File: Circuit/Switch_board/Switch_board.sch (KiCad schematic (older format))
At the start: 10 parts

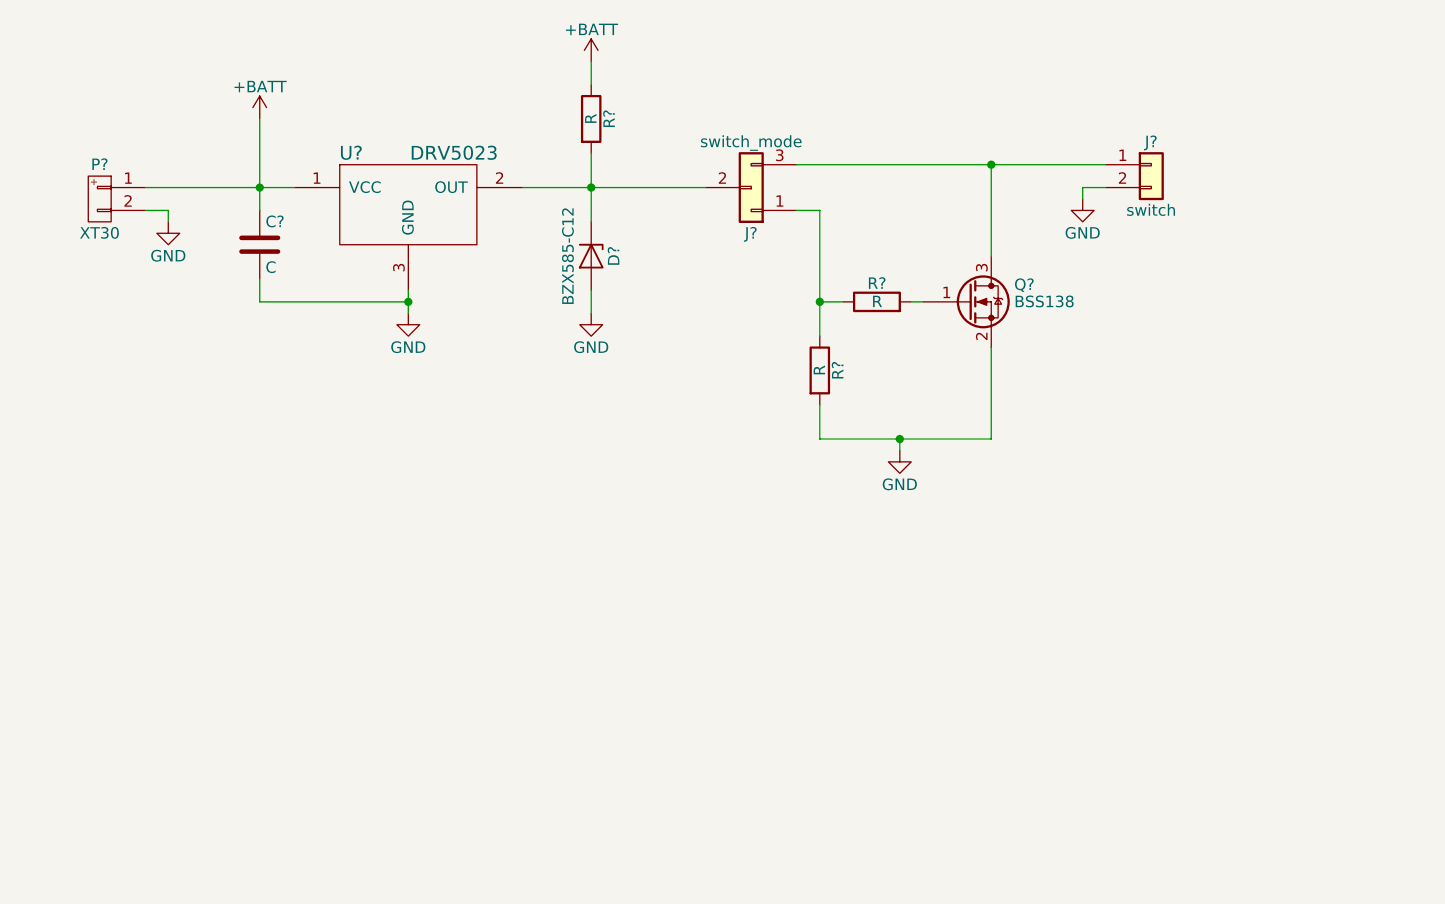
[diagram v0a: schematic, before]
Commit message: switch_board circuit could operate in any switch application without complex config
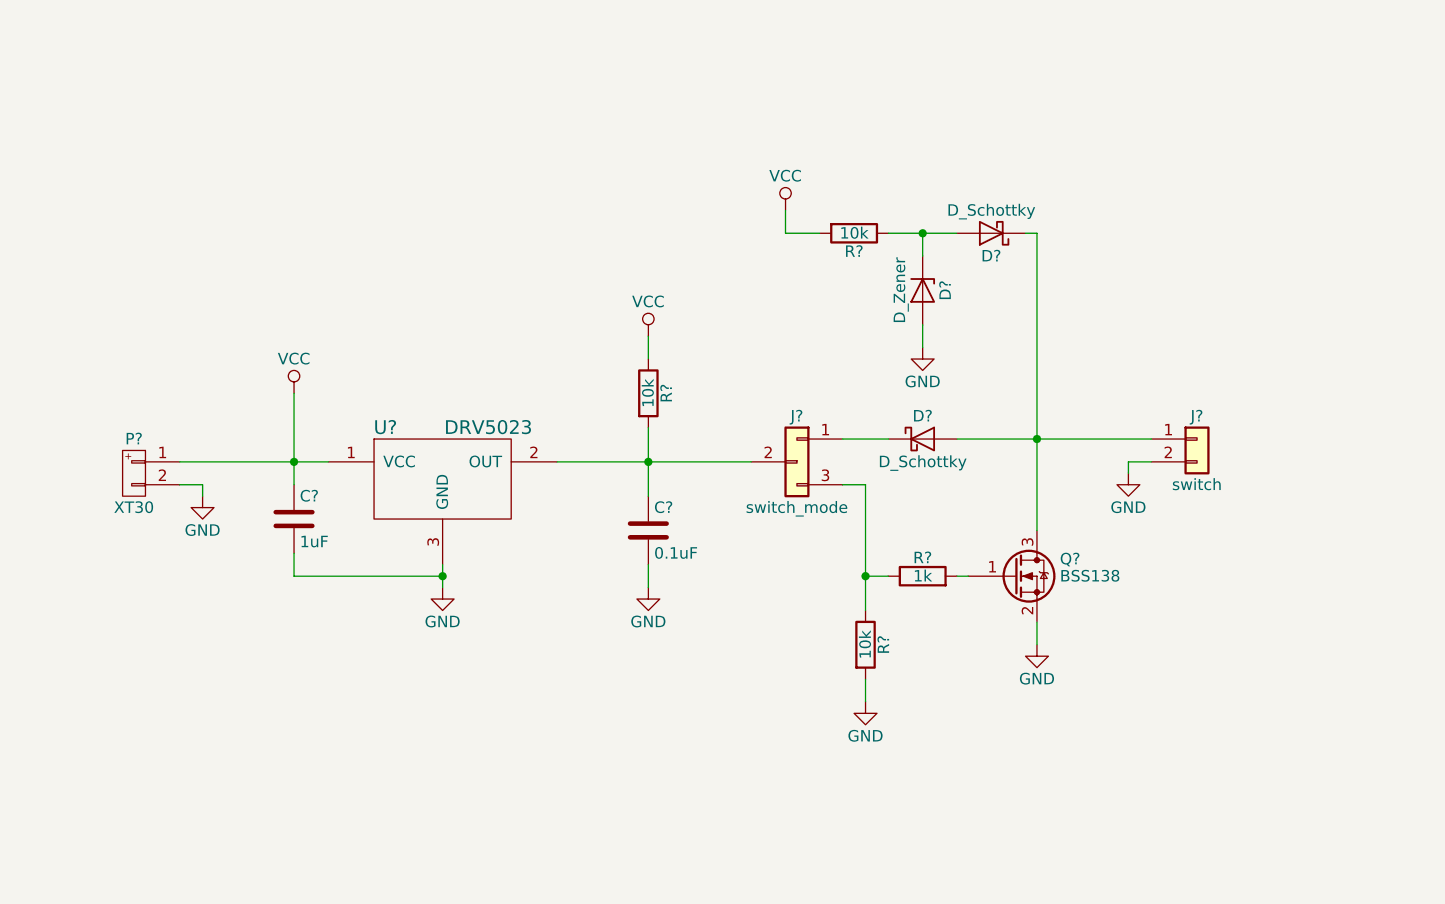
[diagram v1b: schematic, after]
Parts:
- removed D?: BZX585-C12, symbol D_Zener
- added C?: 0.1uF, symbol C
- added D?: D_Zener, symbol D_Zener
- added D? (x2): D_Schottky, symbol D_Schottky
- added R?: 10k, symbol R
- C?: value C -> 1uF
- R? (x2): value R -> 10k
- R?: value R -> 1k
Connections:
- net GND: now also C?.2, D?.2 (A)
- net at J?.2 (Pin_2), R?.2, U?.2 (OUT): now also C?.1
- net at R?.1, R?.1: now also J?.3 (Pin_3); no longer J?.1 (Pin_1)
- net at J?.1 (Pin_1), Q?.3 (D): now also D?.1 (K), D?.2 (A); no longer J?.3 (Pin_3)
- net +BATT renamed VCC
- net VCC: now also R?.2
- new net: D?.1 (K), J?.1 (Pin_1)
- new net: D?.1 (K), D?.2 (A), R?.1
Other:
- moved on the sheet: C?, J?, P?, Q?, R?, U?

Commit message: used double nmos inverter instead of false diode logic
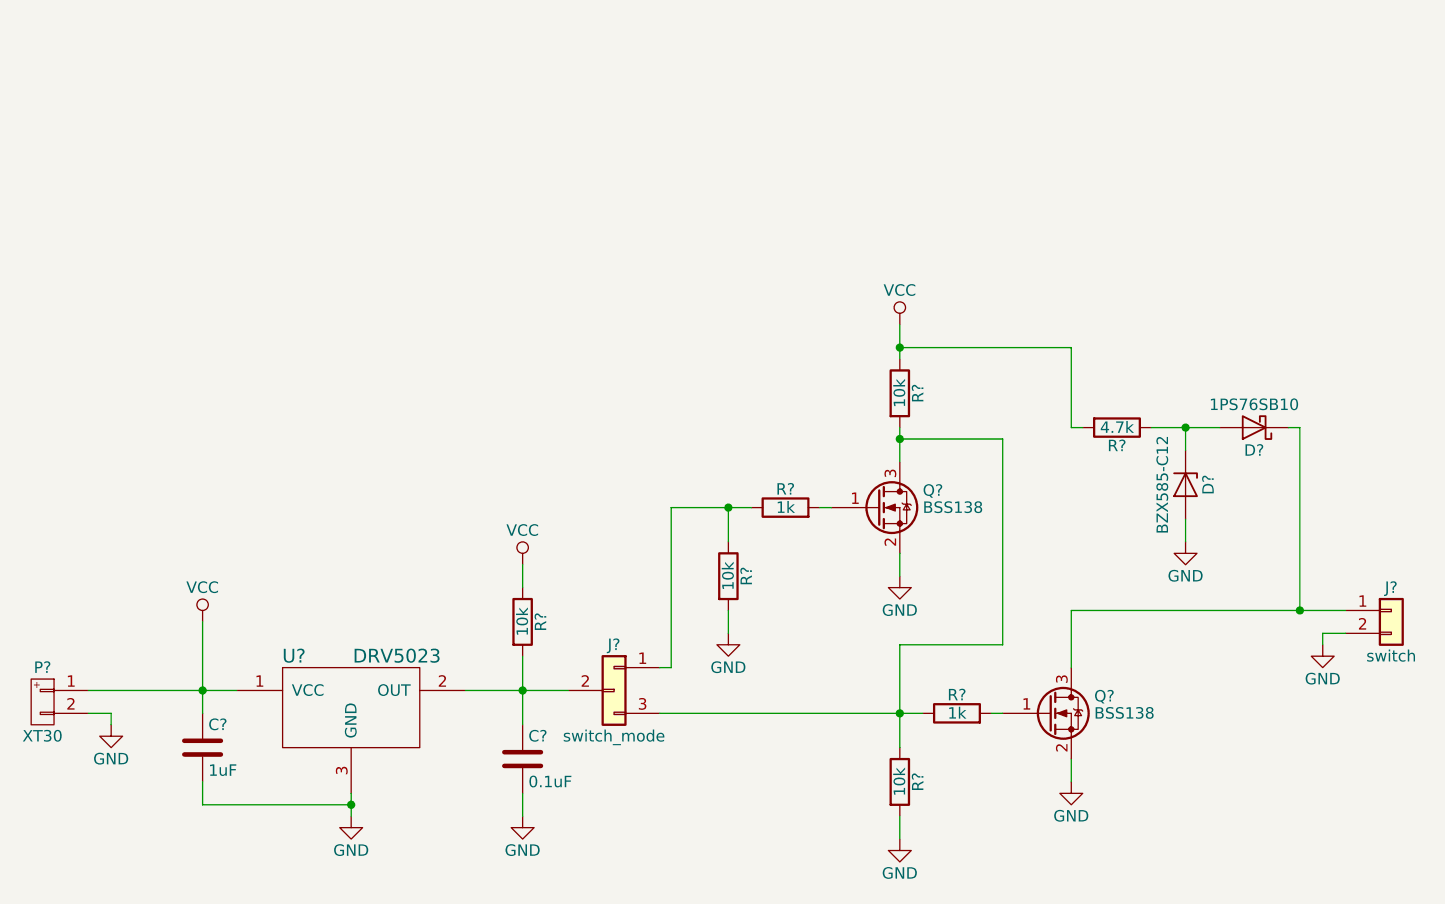
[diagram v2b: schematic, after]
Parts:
- removed D?: D_Schottky, symbol D_Schottky
- added Q?: BSS138, TO_SOT_Packages_SMD:SOT-23, symbol BSS138
- added R? (x2): 10k, symbol R
- added R?: 1k, symbol R
- D?: value D_Zener -> BZX585-C12
- D?: value D_Schottky -> 1PS76SB10
- R?: value 10k -> 4.7k
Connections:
- net GND: now also Q?.2 (S), R?.2
- net VCC: now also R?.1
- net at J?.1 (Pin_1): now also R?.1, R?.1
- net at D?.1 (K), J?.1 (Pin_1): now also Q?.3 (D); no longer Q?.3 (D)
- new net: J?.3 (Pin_3), Q?.3 (D), R?.1, R?.1, R?.2
- new net: Q?.1 (G), R?.2
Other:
- moved on the sheet: C?, D?, J?, P?, Q?, R?, U?

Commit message: assigned footprints on switch_board
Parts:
- C? (x2): footprint (none) -> Capacitors_SMD:C_0603_HandSoldering
- D?: footprint (none) -> Diodes_SMD:D_SOD-523
- D?: footprint (none) -> Diodes_SMD:D_SOD-323_HandSoldering
- J?: footprint (none) -> Pin_Headers:Pin_Header_Straight_1x03_Pitch2.54mm
- J?: footprint (none) -> zeabus:90136-1202
- P?: footprint (none) -> zeabus:XT30
- Q? (x2): footprint TO_SOT_Packages_SMD:SOT-23 -> TO_SOT_Packages_SMD:SOT-23_Handsoldering
- R? (x7): footprint (none) -> Resistors_SMD:R_0603_HandSoldering
- U?: footprint (none) -> TO_SOT_Packages_SMD:SOT-23_Handsoldering
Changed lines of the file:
@@
 F 0 "P?" H 2350 4400 50  0000 C CNN
 F 1 "XT30" H 2350 4100 50  0000 C CNN
-F 2 "" H 2350 4250 60  0001 C CNN
+F 2 "zeabus:XT30" H 2350 4250 60  0001 C CNN
 F 3 "" H 2350 4250 60  0000 C CNN
 	1    2350 4250
@@
 F 0 "U?" H 3450 4350 60  0000 C CNN
 F 1 "DRV5023" H 3900 4350 60  0000 C CNN
-F 2 "" H 3700 4200 60  0001 C CNN
+F 2 "TO_SOT_Packages_SMD:SOT-23_Handsoldering" H 3700 4200 60  0001 C CNN
 F 3 "" H 3700 4200 60  0001 C CNN
 	1    3700 4200
@@
 F 0 "C?" H 3075 4550 50  0000 L CNN
 F 1 "1uF" H 3075 4350 50  0000 L CNN
-F 2 "" H 3088 4300 50  0001 C CNN
+F 2 "Capacitors_SMD:C_0603_HandSoldering" H 3088 4300 50  0001 C CNN
 F 3 "" H 3050 4450 50  0001 C CNN
 	1    3050 4450
@@
 F 0 "R?" V 4530 3900 50  0000 C CNN
 F 1 "10k" V 4450 3900 50  0000 C CNN
-F 2 "" V 4380 3900 50  0001 C CNN
+F 2 "Resistors_SMD:R_0603_HandSoldering" V 4380 3900 50  0001 C CNN
 F 3 "" H 4450 3900 50  0001 C CNN
 	1    4450 3900
@@
 F 0 "J?" H 4850 4400 50  0000 C CNN
 F 1 "switch_mode" H 4850 4000 50  0000 C CNN
-F 2 "" H 4900 4200 50  0001 C CNN
+F 2 "Pin_Headers:Pin_Header_Straight_1x03_Pitch2.54mm" H 4900 4200 50  0001 C CNN
 F 3 "" H 4900 4200 50  0001 C CNN
 	1    4850 4200
@@
 F 0 "J?" H 8250 3950 50  0000 C CNN
 F 1 "switch" H 8250 3650 50  0000 C CNN
-F 2 "" H 8250 3850 50  0001 C CNN
+F 2 "zeabus:90136-1202" H 8250 3850 50  0001 C CNN
 F 3 "" H 8250 3850 50  0001 C CNN
 	1    8250 3850
@@
 F 0 "R?" V 5430 3700 50  0000 C CNN
 F 1 "10k" V 5350 3700 50  0000 C CNN
-F 2 "" V 5280 3700 50  0001 C CNN
+F 2 "Resistors_SMD:R_0603_HandSoldering" V 5280 3700 50  0001 C CNN
 F 3 "" H 5350 3700 50  0001 C CNN
 	1    5350 3700
@@
 F 0 "R?" V 5680 3400 50  0000 C CNN
 F 1 "1k" V 5600 3400 50  0000 C CNN
-F 2 "" V 5530 3400 50  0001 C CNN
+F 2 "Resistors_SMD:R_0603_HandSoldering" V 5530 3400 50  0001 C CNN
 F 3 "" H 5600 3400 50  0001 C CNN
 	1    5600 3400
@@
 F 0 "Q?" H 6200 3475 50  0000 L CNN
 F 1 "BSS138" H 6200 3400 50  0000 L CNN
-F 2 "TO_SOT_Packages_SMD:SOT-23" H 6200 3325 50  0001 L CIN
+F 2 "TO_SOT_Packages_SMD:SOT-23_Handsoldering" H 6200 3325 50  0001 L CIN
 F 3 "" H 6000 3400 50  0001 L CNN
 	1    6000 3400
@@
 F 0 "C?" H 4475 4600 50  0000 L CNN
 F 1 "0.1uF" H 4475 4400 50  0000 L CNN
-F 2 "" H 4488 4350 50  0001 C CNN
+F 2 "Capacitors_SMD:C_0603_HandSoldering" H 4488 4350 50  0001 C CNN
 F 3 "" H 4450 4500 50  0001 C CNN
 	1    4450 4500
@@
 F 0 "R?" V 7130 3050 50  0000 C CNN
 F 1 "4.7k" V 7050 3050 50  0000 C CNN
-F 2 "" V 6980 3050 50  0001 C CNN
+F 2 "Resistors_SMD:R_0603_HandSoldering" V 6980 3050 50  0001 C CNN
 F 3 "" H 7050 3050 50  0001 C CNN
 	1    7050 3050
@@
 F 0 "D?" H 7350 3400 50  0000 C CNN
 F 1 "BZX585-C12" H 7350 3200 50  0000 C CNN
-F 2 "" H 7350 3300 50  0001 C CNN
+F 2 "Diodes_SMD:D_SOD-523" H 7350 3300 50  0001 C CNN
 F 3 "" H 7350 3300 50  0001 C CNN
 	1    7350 3300
@@
 F 0 "D?" H 7650 3150 50  0000 C CNN
 F 1 "1PS76SB10" H 7650 2950 50  0000 C CNN
-F 2 "" H 7650 3050 50  0001 C CNN
+F 2 "Diodes_SMD:D_SOD-323_HandSoldering" H 7650 3050 50  0001 C CNN
 F 3 "" H 7650 3050 50  0001 C CNN
 	1    7650 3050
@@
 F 0 "R?" V 6180 4600 50  0000 C CNN
 F 1 "10k" V 6100 4600 50  0000 C CNN
-F 2 "" V 6030 4600 50  0001 C CNN
+F 2 "Resistors_SMD:R_0603_HandSoldering" V 6030 4600 50  0001 C CNN
 F 3 "" H 6100 4600 50  0001 C CNN
 	1    6100 4600
@@
 F 0 "R?" V 6430 4300 50  0000 C CNN
 F 1 "1k" V 6350 4300 50  0000 C CNN
-F 2 "" V 6280 4300 50  0001 C CNN
+F 2 "Resistors_SMD:R_0603_HandSoldering" V 6280 4300 50  0001 C CNN
 F 3 "" H 6350 4300 50  0001 C CNN
 	1    6350 4300
@@
 F 0 "Q?" H 6950 4375 50  0000 L CNN
 F 1 "BSS138" H 6950 4300 50  0000 L CNN
-F 2 "TO_SOT_Packages_SMD:SOT-23" H 6950 4225 50  0001 L CIN
+F 2 "TO_SOT_Packages_SMD:SOT-23_Handsoldering" H 6950 4225 50  0001 L CIN
 F 3 "" H 6750 4300 50  0001 L CNN
 	1    6750 4300
@@
 F 0 "R?" V 6180 2900 50  0000 C CNN
 F 1 "10k" V 6100 2900 50  0000 C CNN
-F 2 "" V 6030 2900 50  0001 C CNN
+F 2 "Resistors_SMD:R_0603_HandSoldering" V 6030 2900 50  0001 C CNN
 F 3 "" H 6100 2900 50  0001 C CNN
 	1    6100 2900
